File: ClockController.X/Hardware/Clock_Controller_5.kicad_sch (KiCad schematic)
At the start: 2 parts

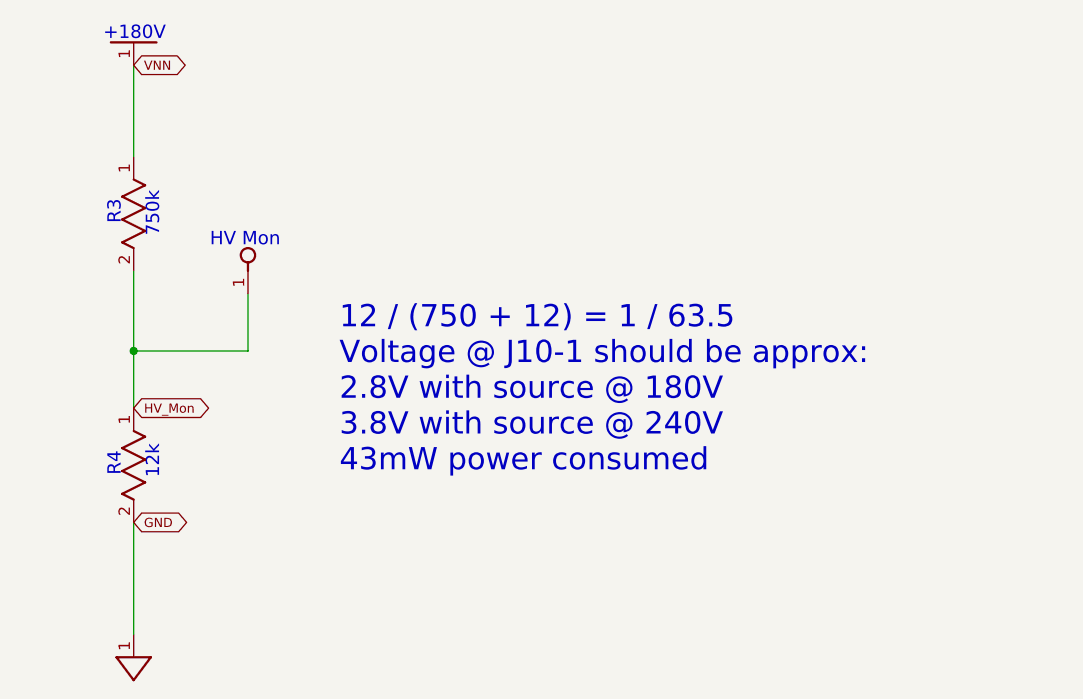
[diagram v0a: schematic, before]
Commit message: Cleaned up a bunch of labels
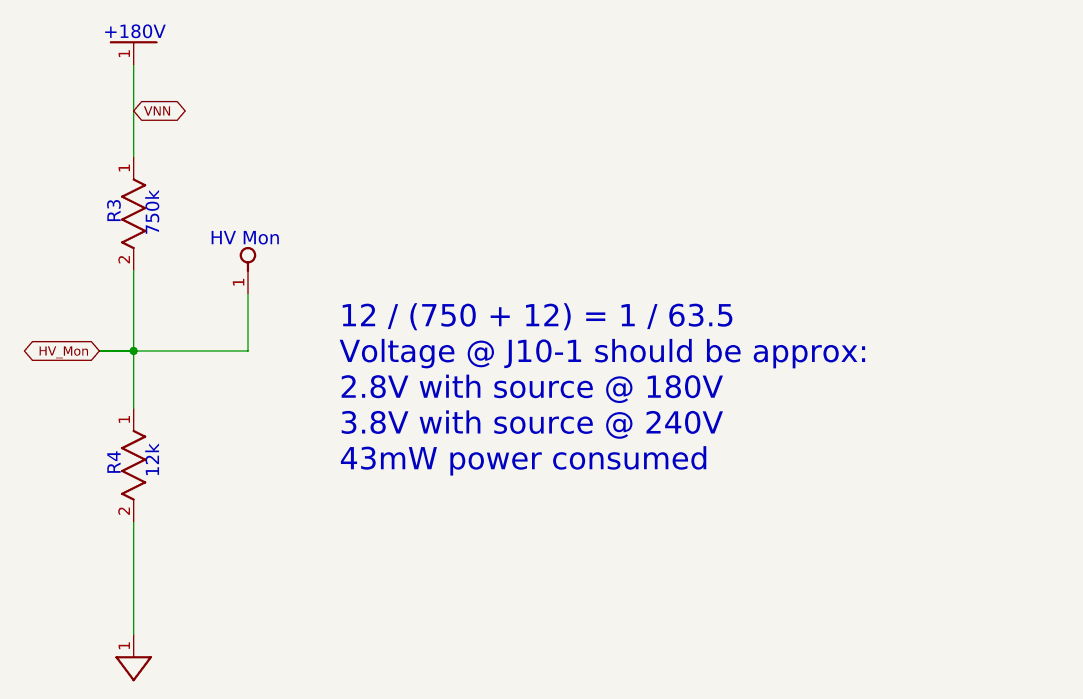
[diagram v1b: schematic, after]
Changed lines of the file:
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@@
 	(wire
 		(pts
-			(xy 102.87 109.22) (xy 102.87 102.87)
+			(xy 99.06 102.87) (xy 102.87 102.87)
+		)
+		(stroke
+			(width 0)
+			(type default)
+		)
+	)
+	(wire
+		(pts
+			(xy 99.06 102.87) (xy 102.87 102.87)
 		)
 		(stroke
@@
 	(wire
 		(pts
-			(xy 102.87 71.12) (xy 102.87 81.28)
+			(xy 102.87 102.87) (xy 102.87 109.22)
+		)
+		(stroke
+			(width 0)
+			(type default)
+		)
+	)
+	(wire
+		(pts
+			(xy 102.87 76.2) (xy 102.87 81.28)
 		)
 		(stroke
 			(width 0.25)
 			(type solid)
+		)
+	)
+	(wire
+		(pts
+			(xy 102.87 76.2) (xy 102.87 71.12)
+		)
+		(stroke
+			(width 0)
+			(type default)
 		)
 	)
@@
 	(global_label "VNN"
 		(shape bidirectional)
-		(at 102.87 71.12 0)
+		(at 102.87 76.2 0)
 		(fields_autoplaced yes)
 		(effects
@@
 		)
 		(property "Intersheetrefs" "${INTERSHEET_REFS}"
-			(at 109.1466 71.12 0)
+			(at 109.1466 76.2 0)
 			(effects
 				(font
@@
 	(global_label "HV_Mon"
 		(shape bidirectional)
-		(at 102.87 109.22 0)
+		(at 99.06 102.87 180)
 		(fields_autoplaced yes)
 		(effects
@@
 				(size 1.016 1.016)
 			)
-			(justify left)
+			(justify right)
 		)
 		(property "Intersheetrefs" "${INTERSHEET_REFS}"
-			(at 111.8558 109.22 0)
+			(at 90.0742 102.87 0)
 			(effects
 				(font
 					(size 1.27 1.27)
 				)
-				(justify left)
+				(justify right)
 				(hide yes)
 			)
-		)
-	)
-	(global_label "GND"
-		(shape bidirectional)
-		(at 102.87 121.92 0)
-		(fields_autoplaced yes)
-		(effects
-			(font
-				(size 1.016 1.016)
-			)
-			(justify left)
-		)
-		(property "Intersheetrefs" "${INTERSHEET_REFS}"
-			(at 109.2433 121.92 0)
-			(effects
-				(font
-					(size 1.27 1.27)
-				)
-				(justify left)
-				(hide yes)
-			)
